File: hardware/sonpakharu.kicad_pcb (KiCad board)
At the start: 2 copper layers, 51.3 x 71.1 mm, 64 parts, among them IC1 ESP32-S3-WROOM-1U-N4, J1 ADC4, J10 EXT2, J11 EXT3, J12 BATT, J13 EXT7, J14 PWR, J15 EXT8, J16 FTDI, J17 485, J2 ADC3, J3 ADC2, J4 ADC1, J5 EXT4, J6 I2C, J7 EXT5, J8 EXT1, J9 EXT6, Q1 DMG3415U, Q2 S8050, Q3 S8050, Q4 S8050, SW1 Boot, SW2 Reset, U1 AP2112K-3.3TRG1, U2 MCP73831-2-OT, U3 ADS1115IDGSR, U4 MAX485E

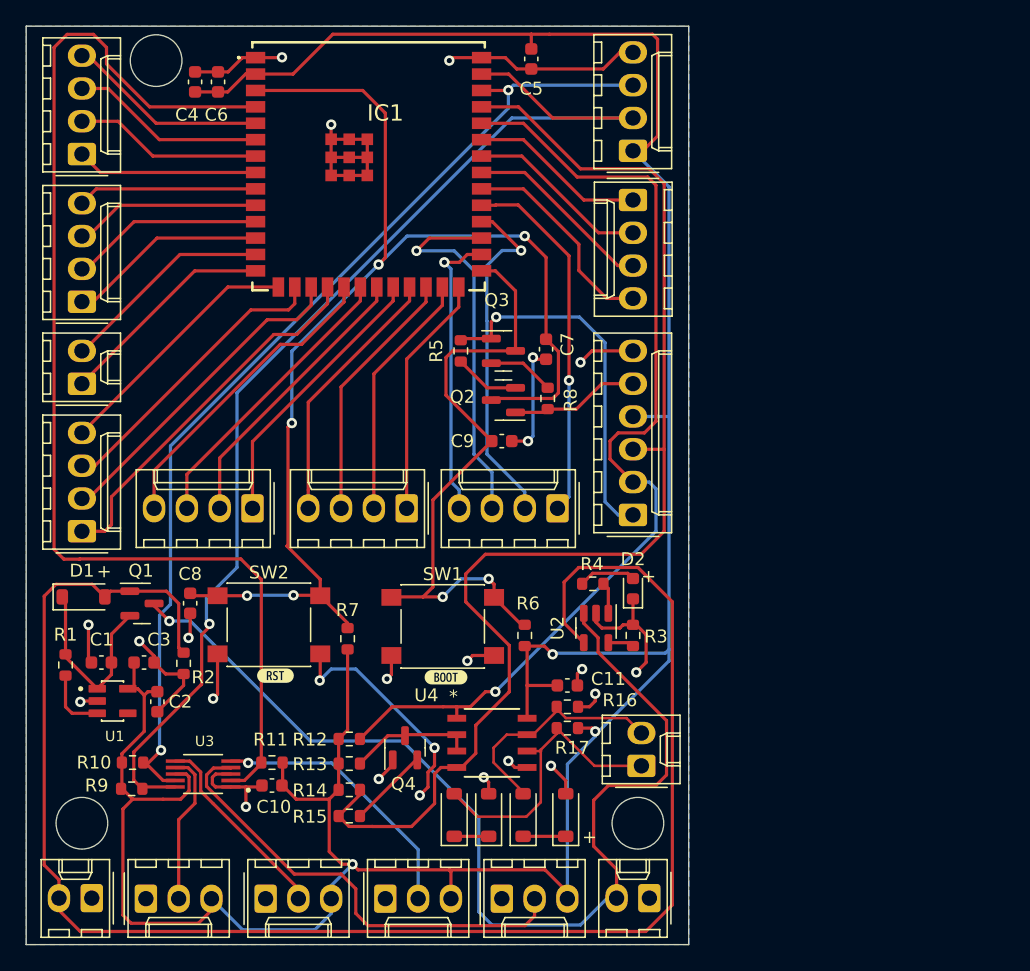
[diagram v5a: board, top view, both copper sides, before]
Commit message: Fix: added pads, ground vias and logo
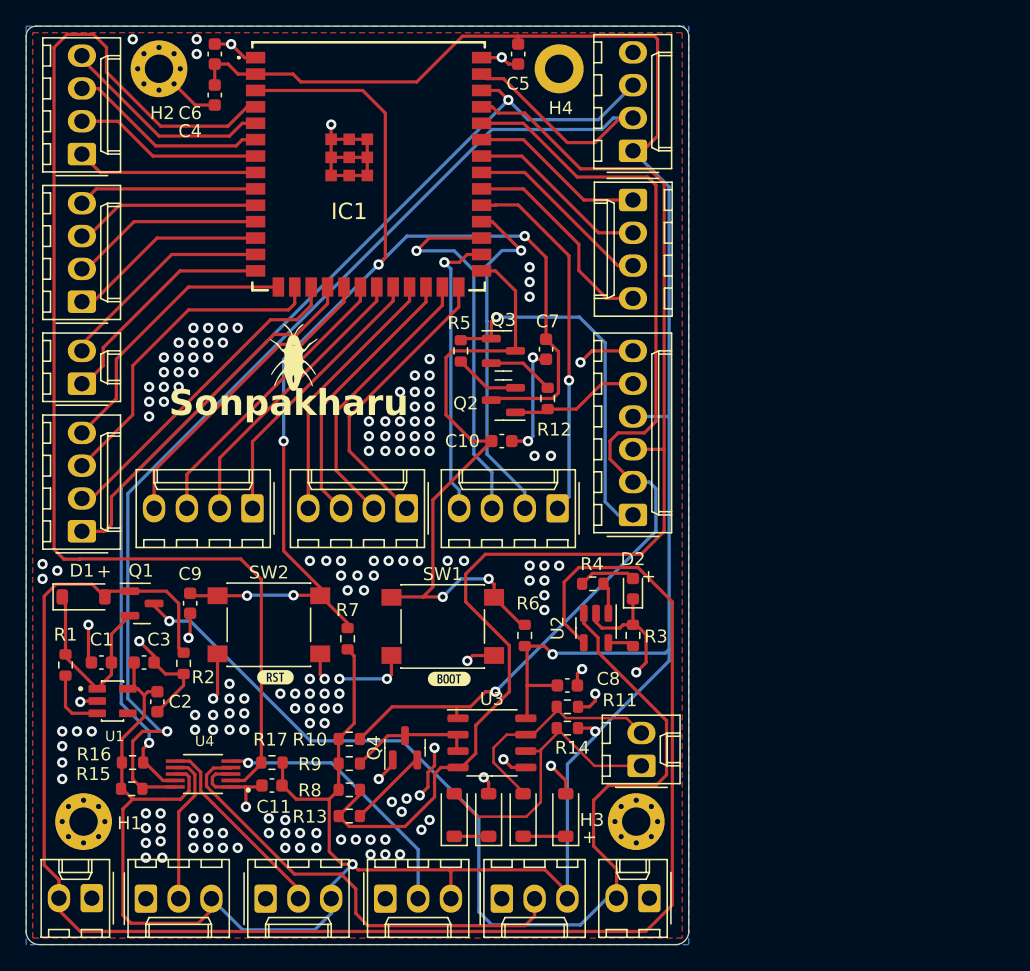
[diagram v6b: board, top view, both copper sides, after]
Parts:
- added G***: LOGO, logo:sonpakaharu, F.Cu at (126.6, 63.2)
- added G***: LOGO, logo:sonpakaharu, B.Cu at (123.2, 49.1)
- added H1: MountingHole_Pad, MountingHole:MountingHole_2.2mm_M2_Pad_Via, F.Cu at (110.4, 99.2)
- added H2: MountingHole_Pad, MountingHole:MountingHole_2.2mm_M2_Pad_Via, F.Cu at (116.2, 40.9)
- added H3: MountingHole_Pad, MountingHole:MountingHole_2.2mm_M2_Pad_Via, F.Cu at (153.2, 99.2)
- added H4: MountingHole_Pad, MountingHole:MountingHole_2.2mm_M2_DIN965_Pad, F.Cu at (147.2, 40.9)
- IC1: footprint RF_Module:ESP32S3WROOM1UN4 -> KiCad:ESP32S3WROOM1UN4
- U3: renamed from U4; footprint MAX485SOIC8:21-0041B_8_MXM -> Package_SO:SOP-8_3.9x4.9mm_P1.27mm
- moved C6 2.17 mm to (120.5, 39.8)
- moved C4 1.83 mm to (120.5, 42.9), turned to -90 degrees
- moved C5 1.09 mm to (144.0, 39.8)
- moved kibuzzard-659587ED 0.28 mm to (138.7, 88.1)
- moved kibuzzard-659587E1 0.13 mm to (125.2, 88.0)
- renumbered C9 to C10, C10 to C11, C11 to C8, C8 to C9, D5 to D4, D4 to D5, J17 to J16, J16 to J17, R12 to R10, R16 to R11, R8 to R12, R15 to R13, R17 to R14, R9 to R15, R10 to R16, R11 to R17, R14 to R8, R13 to R9, U3 to U4
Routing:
- net GND: track 120.8 -> 103.5 mm, vias 24 -> 168
- net /SCL: track 89.7 -> 95.4 mm
- net /GP22: track 18.8 -> 22.5 mm
- net /SDA: track 78.9 -> 81.6 mm
- net /GP21: track 19.3 -> 21.8 mm
- net /GP12: track 23.0 -> 25.2 mm
- net /GP11: track 19.9 -> 21.7 mm
- net /IO4: track 92.2 -> 93.8 mm
- net /GP20: track 19.9 -> 21.1 mm
- net /GP1: track 15.6 -> 16.6 mm
- net /IO0: track 48.5 -> 49.3 mm
- net /GP10: track 17.1 -> 17.9 mm
- added copper zone on F.Cu, net GND
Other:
- outline, holes or cut-outs redrawn
- board text added: "Sonpakharu"

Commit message: updated tactile smd part number
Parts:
- added SW1: Boot, Button_Switch_SMD:SW_Push_1P1T_NO_6x6mm_H9.5mm, F.Cu at (176.9, 52.8)
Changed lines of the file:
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@@
     (descr "tactile push button, 6x6mm e.g. PTS645xx series, height=9.5mm")
     (tags "tact sw push 6mm smd")
-    (property "MPN" "C116647")
+    (property "MPN" "C285446")
     (property "Sheetfile" "sonpakharu.kicad_sch")
     (property "Sheetname" "")
@@
     (descr "tactile push button, 6x6mm e.g. PTS645xx series, height=9.5mm")
     (tags "tact sw push 6mm smd")
-    (property "MPN" "C116647")
+    (property "MPN" "C285446")
     (property "Sheetfile" "sonpakharu.kicad_sch")
     (property "Sheetname" "")
@@
       (net 2 "GND") (pinfunction "1") (pintype "input"))
   )
+  (footprint "Button_Switch_SMD:SW_Push_1P1T_NO_6x6mm_H9.5mm" (layer "F.Cu")
+    (at 176.911 52.832)
+    (descr "tactile push button, 6x6mm e.g. PTS645xx series, height=9.5mm")
+    (tags "tact sw push 6mm smd")
+    (property "MPN" "C116647")
+    (property "Sheetfile" "sonpakharu.kicad_sch")
+    (property "Sheetname" "")
+    (property "ki_description" "Push button switch, generic, two pins")
+    (property "ki_keywords" "switch normally-open pushbutton push-button")
+    (attr smd)
+    (fp_text reference "SW1" (at 0 -4.05) (layer "F.SilkS")
+        (effects (font (size 1 1) (thickness 0.15)))
+    )
+    (fp_text value "Boot" (at 0 4.15) (layer "F.Fab")
+        (effects (font (size 1 1) (thickness 0.15)))
+    )
+    (fp_text user "${REFERENCE}" (at 0 -4.05) (layer "F.Fab")
+        (effects (font (size 1 1) (thickness 0.15)))
+    )
+    (fp_line (start -3.23 -3.23) (end 3.23 -3.23)
+      (stroke (width 0.12) (type solid)) (layer "F.SilkS"))
+    (fp_line (start -3.23 -3.2) (end -3.23 -3.23)
+      (stroke (width 0.12) (type solid)) (layer "F.SilkS"))
+    (fp_line (start -3.23 -1.3) (end -3.23 1.3)
+      (stroke (width 0.12) (type solid)) (layer "F.SilkS"))
+    (fp_line (start -3.23 3.23) (end -3.23 3.2)
+      (stroke (width 0.12) (type solid)) (layer "F.SilkS"))
+    (fp_line (start -3.23 3.23) (end 3.23 3.23)
+      (stroke (width 0.12) (type solid)) (layer "F.SilkS"))
+    (fp_line (start 3.23 -3.23) (end 3.23 -3.2)
+      (stroke (width 0.12) (type solid)) (layer "F.SilkS"))
+    (fp_line (start 3.23 -1.3) (end 3.23 1.3)
+      (stroke (width 0.12) (type solid)) (layer "F.SilkS"))
+    (fp_line (start 3.23 3.23) (end 3.23 3.2)
+      (stroke (width 0.12) (type solid)) (layer "F.SilkS"))
+    (fp_line (start -5 -3.25) (end -5 3.25)
+      (stroke (width 0.05) (type solid)) (layer "F.CrtYd"))
+    (fp_line (start -5 -3.25) (end 5 -3.25)
+      (stroke (width 0.05) (type solid)) (layer "F.CrtYd"))
+    (fp_line (start -5 3.25) (end 5 3.25)
+      (stroke (width 0.05) (type solid)) (layer "F.CrtYd"))
+    (fp_line (start 5 3.25) (end 5 -3.25)
+      (stroke (width 0.05) (type solid)) (layer "F.CrtYd"))
+    (fp_line (start -3 -3) (end -3 3)
+      (stroke (width 0.1) (type solid)) (layer "F.Fab"))
+    (fp_line (start -3 3) (end 3 3)
+      (stroke (width 0.1) (type solid)) (layer "F.Fab"))
+    (fp_line (start 3 -3) (end -3 -3)
+      (stroke (width 0.1) (type solid)) (layer "F.Fab"))
+    (fp_line (start 3 3) (end 3 -3)
+      (stroke (width 0.1) (type solid)) (layer "F.Fab"))
+    (fp_circle (center 0 0) (end 1.75 -0.05)
+      (stroke (width 0.1) (type solid)) (fill none) (layer "F.Fab"))
+    (pad "1" smd rect (at -3.975 -2.25) (size 1.55 1.3) (layers "F.Cu" "F.Paste" "F.Mask")
+      (pinfunction "1") (pintype "passive"))
+    (pad "1" smd rect (at 3.975 -2.25) (size 1.55 1.3) (layers "F.Cu" "F.Paste" "F.Mask")
+      (pinfunction "1") (pintype "passive"))
+    (pad "2" smd rect (at -3.975 2.25) (size 1.55 1.3) (layers "F.Cu" "F.Paste" "F.Mask")
+      (pinfunction "2") (pintype "passive"))
+    (pad "2" smd rect (at 3.975 2.25) (size 1.55 1.3) (layers "F.Cu" "F.Paste" "F.Mask")
+      (pinfunction "2") (pintype "passive"))
+    (model "${KICAD6_3DMODEL_DIR}/Button_Switch_SMD.3dshapes/SW_PUSH_6mm_H9.5mm.wrl"
+      (offset (xyz 0 0 0))
+      (scale (xyz 1 1 1))
+      (rotate (xyz 0 0 0))
+    )
+  )
   (footprint "logo:sonpakaharu" (layer "B.Cu")

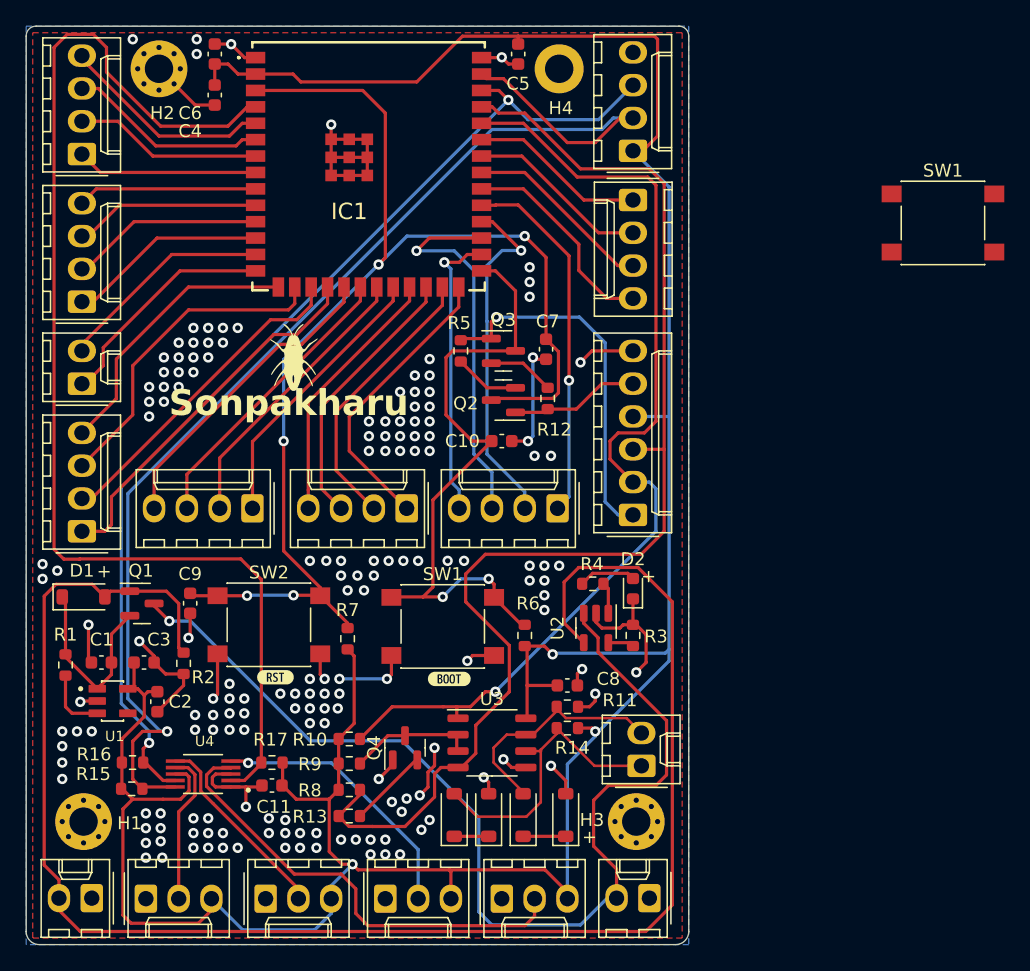
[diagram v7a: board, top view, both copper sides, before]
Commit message: Fix: foot prints, re routed pcb, added 3d model
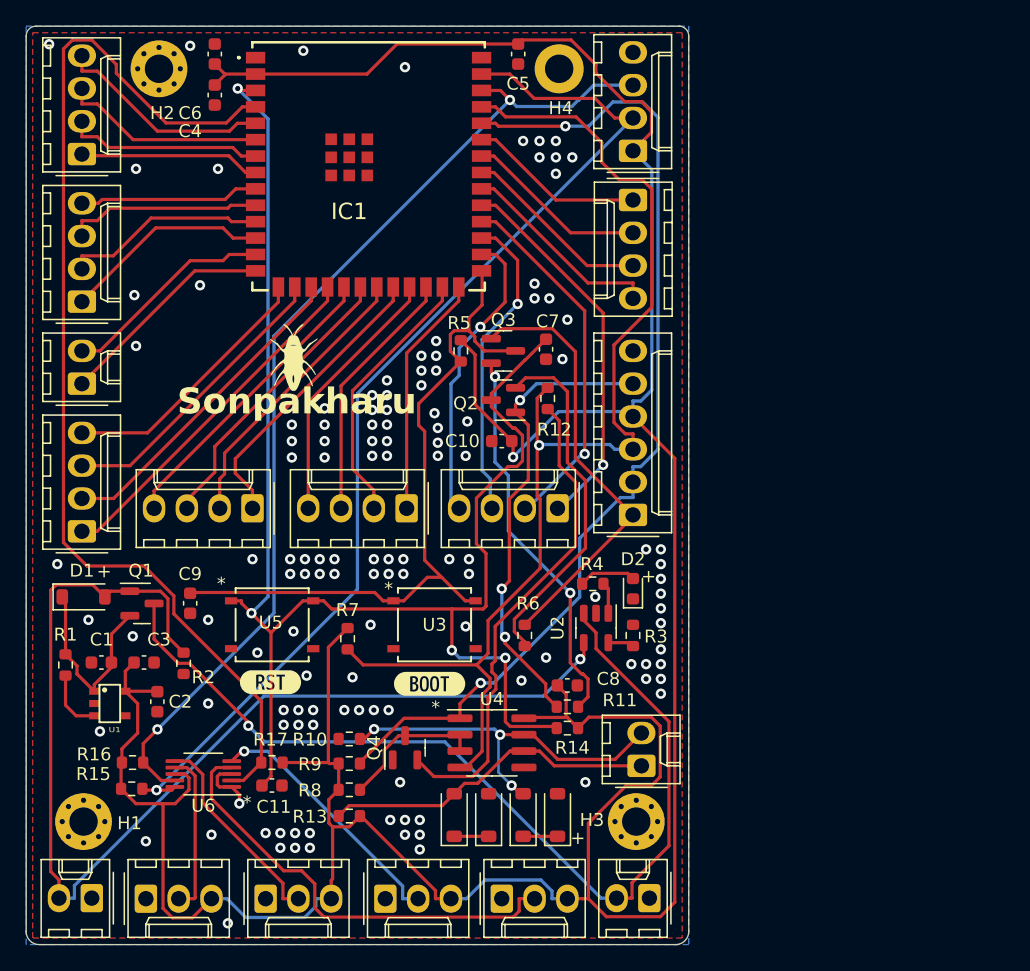
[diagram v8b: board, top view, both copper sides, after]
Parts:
- removed SW1 (x2): Boot, Button_Switch_SMD:SW_Push_1P1T_NO_6x6mm_H9.5mm
- removed SW2: Reset, Button_Switch_SMD:SW_Push_1P1T_NO_6x6mm_H9.5mm
- removed kibuzzard-659587E1: G***, kibuzzard-659587E1
- removed kibuzzard-659587ED: G***, kibuzzard-659587ED
- added U5: Reset, PTS526 SK15 SMTR2 LFS:SMT_FS, F.Cu at (125.0, 83.9)
- added U6: ADS1115IDGSR, Package_SO:VSSOP-10_3x3mm_P0.5mm, F.Cu at (119.6, 95.5)
- added kibuzzard-65BFB976: G***, kibuzzard-65BFB976, F.Cu at (137.2, 88.5)
- added kibuzzard-65BFB983: G***, kibuzzard-65BFB983, F.Cu at (124.8, 88.4)
- H2: value MountingHole_Pad -> mounting hole
- Q3: value S8050 -> SS8050-G
- R10, R13: value 10K -> 20K
- R11: value 20K -> 12K
- R12, R5: value 12K -> 10K
- R14: value 20K -> 10K
- R6: value 10K -> 12K
- U1: footprint AP2112K-3.3TRG1:SOT95P285X140-5N -> AP2112K_3_3TRG1:SOT25
- U3: value MAX485E -> Boot; footprint Package_SO:SOP-8_3.9x4.9mm_P1.27mm -> PTS526 SK15 SMTR2 LFS:SMT_FS
- U4: value ADS1115IDGSR -> MAX485E; footprint ADS1115IDGSR:SOP50P490X110-10N -> Package_SO:SOIC-8_3.9x4.9mm_P1.27mm
- moved U4 22.5 mm to (142.0, 93.1), turned to 0 degrees
- moved U3 10.2 mm to (137.5, 83.9)
- moved spb 7.88 mm to (131.1, 49.4)
- moved D6 0.63 mm to (147.1, 98.7)
- moved U1 0.29 mm to (112.4, 90.0), turned to -90 degrees
- renumbered G*** to sp, G*** to spb
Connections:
- C10 pad 1: /IO0 -> GND
- C10 pad 2: GND -> +3V3
- C11 pad 1: GND -> /EN
- C11 pad 2: +3V3 -> GND
- C9 pad 1: /EN -> /IO0
- R10 pad 1: +3V3 -> GND
- R10 pad 2: /RX -> /D-
- R11 pad 1: GND -> Net-(Q3-B)
- R11 pad 2: /D- -> /RTS
- R12 pad 1: Net-(Q3-B) -> /TX
- R12 pad 2: /RTS -> Net-(Q4-B)
- R13 pad 1: /TX -> /D+
- R13 pad 2: Net-(Q4-B) -> +3V3
- R14 pad 1: /D+ -> /EN
- R5 pad 1: Net-(Q2-B) -> /IO0
- R5 pad 2: /DTR -> +3V3
- R6 pad 1: +3V3 -> Net-(Q2-B)
- R6 pad 2: /IO0 -> /DTR
- R7 pad 1: /EN -> +3V3
- R7 pad 2: +3V3 -> /TX
- R8 pad 2: /TX -> Net-(Q4-C)
- R9 pad 2: Net-(Q4-C) -> /RX
- U1 pad 4: (no net) -> unconnected-(U1-NC-Pad4)
- U3 pad 1: /RX -> /IO0
- U3 pad 2: Net-(Q4-C) -> /IO0
- U3 pad 3: Net-(Q4-C) -> GND
- U3 pad 4: /TX -> GND
- U4 pad 1: GND -> /RX
- U4 pad 2: /IO4 -> Net-(Q4-C)
- U4 pad 3: GND -> Net-(Q4-C)
- U4 pad 4: /A0 -> /TX
- U4 pad 5: /A1 -> GND
- U4 pad 6: /A2 -> /D+
- U4 pad 7: /A3 -> /D-
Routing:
- net GND: track 103.5 -> 4.55 mm, vias 168 -> 127
- net VBUS: track 128.3 -> 88.8 mm, vias 0 -> 1
- net Net-(Q4-B): track 6.24 -> 37.7 mm
- net +3V3: track 233.3 -> 260.6 mm, vias 3 -> 1
- net /RTS: track 10.0 -> 36.2 mm, vias 0 -> 3
- net Net-(Q3-B): track 5.16 -> 30.1 mm, vias 0 -> 2
- net /EN: track 97.0 -> 120.4 mm, vias 5 -> 4
- net Net-(Q2-B): track 5.08 -> 27.7 mm
- net /SCL: track 95.4 -> 83.1 mm
- net /D-: track 18.2 -> 29.5 mm, vias 0 -> 3
- net /IO4: track 93.8 -> 85.8 mm
- net +BATT: track 81.3 -> 74.2 mm
- net /IO0: track 49.3 -> 56.2 mm, vias 2 -> 0
- net /DTR: track 28.4 -> 34.0 mm, vias 1 -> 0
- net /TX: track 96.1 -> 90.7 mm, vias 0 -> 1
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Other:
- board text added: "*"
